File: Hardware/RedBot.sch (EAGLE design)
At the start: 67 parts, among them U1 ATMEGA328P, U2 TB6612FNG, U3 MIC5219 5V, U4 MIC5219 3.3V, U5 FT232RLSSOP, U6 7408SE, Y1 16MHz

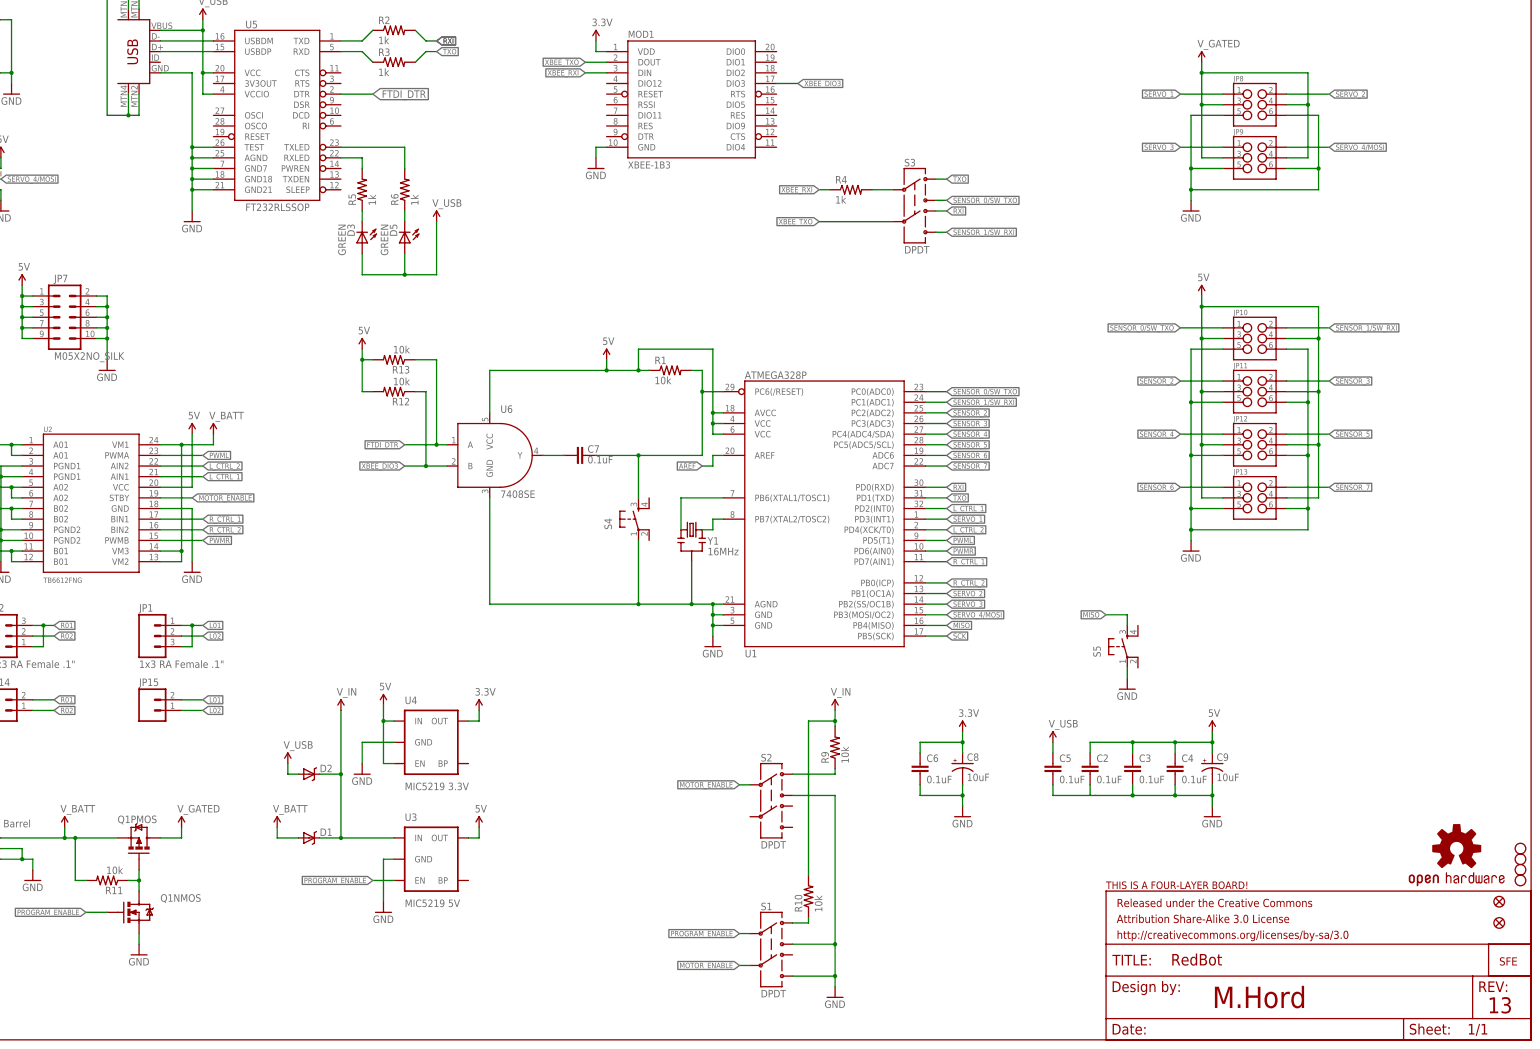
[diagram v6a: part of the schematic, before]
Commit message: Rollback design to current master
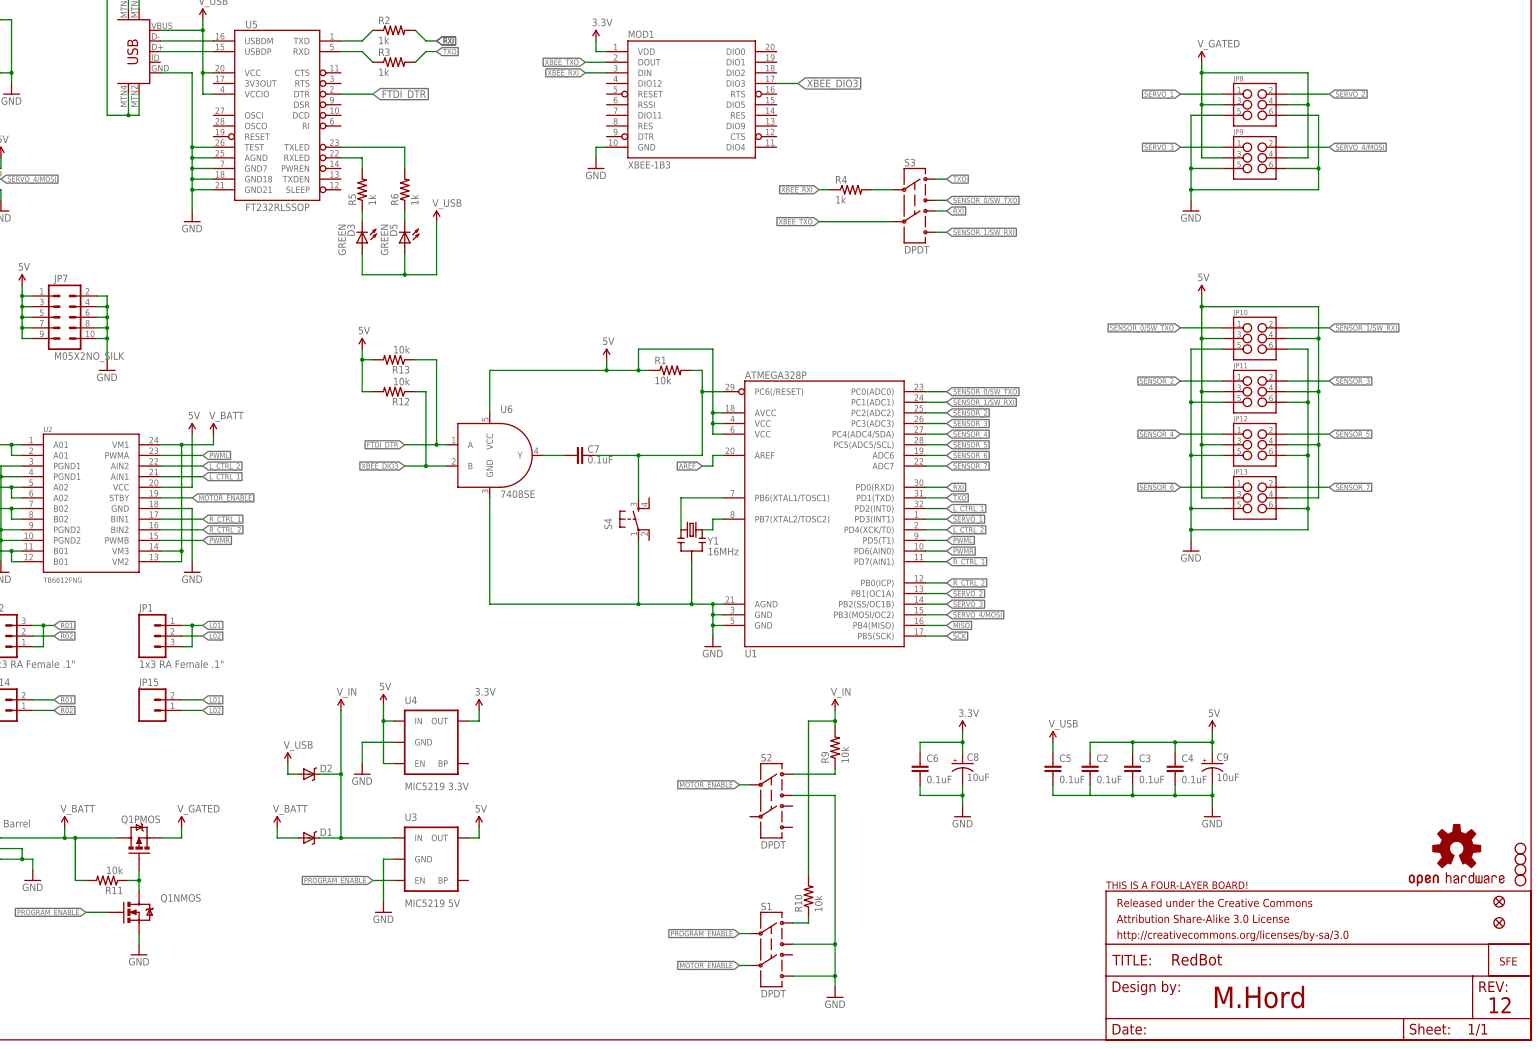
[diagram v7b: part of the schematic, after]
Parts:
- removed S5: (no value), SparkFun-Electromechanical:TAC_SWITCHSMD
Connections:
- net GND: no longer S5.1
- net MISO: no longer S5.3
- net V_BATT: now also Q1PMOS.D; no longer Q1PMOS.S
- net V_GATED: now also Q1PMOS.S; no longer Q1PMOS.D
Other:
- note added: "12"
- note removed: "13"
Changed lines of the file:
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@@
 <layer number="106" name="bPlate" color="7" fill="1" visible="no" active="yes"/>
 <layer number="107" name="Crop" color="7" fill="1" visible="no" active="yes"/>
-<layer number="108" name="tplace-old" color="10" fill="1" visible="yes" active="yes"/>
-<layer number="109" name="ref-old" color="11" fill="1" visible="yes" active="yes"/>
 <layer number="116" name="Patch_BOT" color="9" fill="4" visible="no" active="yes"/>
 <layer number="121" name="_tsilk" color="7" fill="1" visible="no" active="yes"/>
@@
 <part name="FID2" library="SparkFun-Aesthetics" deviceset="FIDUCIAL" device="UFIDUCIAL"/>
 <part name="U$22" library="SparkFun-Aesthetics" deviceset="5V" device="" value="V_USB"/>
-<part name="S5" library="SparkFun-Electromechanical" deviceset="TAC_SWITCH" device="SMD"/>
-<part name="GND12" library="SparkFun-Aesthetics" deviceset="GND" device=""/>
 </parts>
 <sheets>
@@
 <wire x1="0" y1="254" x2="0" y2="0" width="0.1524" layer="94"/>
 <text x="330.2" y="7.62" size="5.08" layer="94">M.Hord</text>
-<text x="395.986" y="6.35" size="3.81" layer="94">13</text>
+<text x="395.986" y="6.35" size="3.81" layer="94">12</text>
 </plain>
 <instances>
@@
 <instance part="JP15" gate="G$1" x="76.2" y="78.74"/>
 <instance part="Q1" gate="NMOS" x="73.66" y="30.48"/>
-<instance part="Q1" gate="PMOS" x="73.66" y="48.26" smashed="yes" rot="MR90">
-<attribute name="NAME" x="77.978" y="51.816" size="1.778" layer="95" rot="MR0"/>
-<attribute name="VALUE" x="73.66" y="53.34" size="1.778" layer="96" rot="MR90"/>
+<instance part="Q1" gate="PMOS" x="73.66" y="48.26" smashed="yes" rot="R90">
+<attribute name="NAME" x="69.342" y="51.816" size="1.778" layer="95"/>
+<attribute name="VALUE" x="73.66" y="53.34" size="1.778" layer="96" rot="R90"/>
 </instance>
 <instance part="GND19" gate="1" x="73.66" y="20.32"/>
@@
 <instance part="FID2" gate="G$1" x="398.78" y="27.94"/>
 <instance part="U$22" gate="G$1" x="144.78" y="195.58"/>
-<instance part="S5" gate="S" x="309.88" y="93.98" rot="R90"/>
-<instance part="GND12" gate="1" x="309.88" y="83.82"/>
 </instances>
 <busses>
@@
 <wire x1="20.32" y1="208.28" x2="15.24" y2="208.28" width="0.1524" layer="91"/>
 <label x="15.24" y="208.28" size="1.27" layer="95" rot="R180" xref="yes"/>
-</segment>
-<segment>
-<pinref part="S5" gate="S" pin="3"/>
-<wire x1="309.88" y1="99.06" x2="309.88" y2="101.6" width="0.1524" layer="91"/>
-<wire x1="309.88" y1="101.6" x2="304.8" y2="101.6" width="0.1524" layer="91"/>
-<label x="304.8" y="101.6" size="1.27" layer="95" rot="R180" xref="yes"/>
 </segment>
 </net>
@@
 <wire x1="27.94" y1="22.86" x2="27.94" y2="20.32" width="0.1524" layer="91"/>
 </segment>
-<segment>
-<pinref part="GND12" gate="1" pin="GND"/>
-<pinref part="S5" gate="S" pin="1"/>
-<wire x1="309.88" y1="86.36" x2="309.88" y2="88.9" width="0.1524" layer="91"/>
-</segment>
 </net>
 <net name="5V" class="0">
@@
 <wire x1="60.96" y1="38.1" x2="58.42" y2="38.1" width="0.1524" layer="91"/>
 <wire x1="58.42" y1="38.1" x2="58.42" y2="48.26" width="0.1524" layer="91"/>
+<pinref part="Q1" gate="PMOS" pin="D"/>
+<wire x1="58.42" y1="48.26" x2="68.58" y2="48.26" width="0.1524" layer="91"/>
+<junction x="58.42" y="48.26"/>
 <wire x1="40.64" y1="48.26" x2="55.88" y2="48.26" width="0.1524" layer="91"/>
 <pinref part="U$18" gate="G$1" pin="V_BATT"/>
@@
 <wire x1="55.88" y1="50.8" x2="55.88" y2="48.26" width="0.1524" layer="91"/>
 <junction x="55.88" y="48.26"/>
-<pinref part="Q1" gate="PMOS" pin="S"/>
-<wire x1="68.58" y1="48.26" x2="58.42" y2="48.26" width="0.1524" layer="91"/>
-<junction x="58.42" y="48.26"/>
 </segment>
 <segment>
@@
 <pinref part="MOD1" gate="G$1" pin="DIO3"/>
 <wire x1="226.06" y1="228.6" x2="231.14" y2="228.6" width="0.1524" layer="91"/>
-<label x="231.14" y="228.6" size="1.27" layer="95" xref="yes"/>
+<label x="231.14" y="228.6" size="1.778" layer="95" xref="yes"/>
 </segment>
 <segment>
@@
 <net name="V_GATED" class="0">
 <segment>
+<pinref part="Q1" gate="PMOS" pin="S"/>
+<wire x1="78.74" y1="48.26" x2="83.82" y2="48.26" width="0.1524" layer="91"/>
 <pinref part="V_GATE1" gate="G$1" pin="V_BATT"/>
 <wire x1="83.82" y1="50.8" x2="83.82" y2="48.26" width="0.1524" layer="91"/>
-<pinref part="Q1" gate="PMOS" pin="D"/>
-<wire x1="78.74" y1="48.26" x2="83.82" y2="48.26" width="0.1524" layer="91"/>
-</segment>
-<segment>
+</segment>
+<segment>

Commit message: Update boards to v13. - Flip MOSFET to gate power to Servo headers - Add button to pin 12 - change silk on LED to D13 LED - add some silk to the back
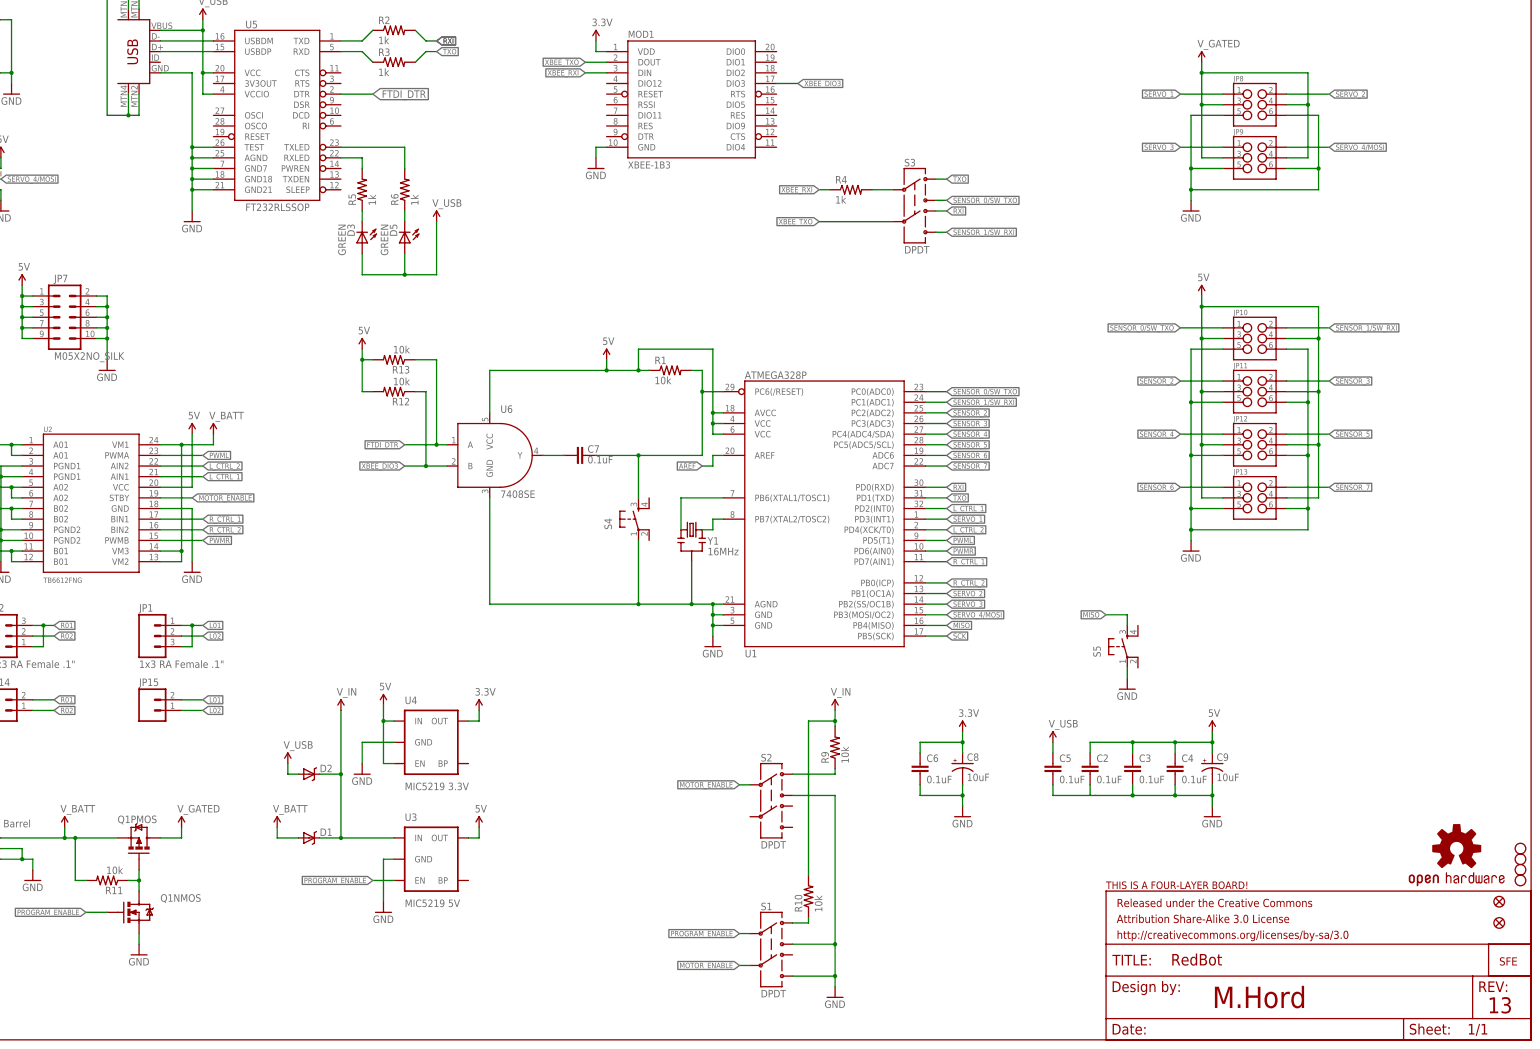
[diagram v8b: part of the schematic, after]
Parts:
- added S5: (no value), SparkFun-Electromechanical:TAC_SWITCHSMD
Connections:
- net GND: now also S5.1
- net MISO: now also S5.3
- net V_BATT: now also Q1PMOS.S; no longer Q1PMOS.D
- net V_GATED: now also Q1PMOS.D; no longer Q1PMOS.S
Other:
- note added: "13"
- note removed: "12"
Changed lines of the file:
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@@
 <layer number="106" name="bPlate" color="7" fill="1" visible="no" active="yes"/>
 <layer number="107" name="Crop" color="7" fill="1" visible="no" active="yes"/>
+<layer number="108" name="tplace-old" color="10" fill="1" visible="yes" active="yes"/>
+<layer number="109" name="ref-old" color="11" fill="1" visible="yes" active="yes"/>
 <layer number="116" name="Patch_BOT" color="9" fill="4" visible="no" active="yes"/>
 <layer number="121" name="_tsilk" color="7" fill="1" visible="no" active="yes"/>
@@
 <part name="FID2" library="SparkFun-Aesthetics" deviceset="FIDUCIAL" device="UFIDUCIAL"/>
 <part name="U$22" library="SparkFun-Aesthetics" deviceset="5V" device="" value="V_USB"/>
+<part name="S5" library="SparkFun-Electromechanical" deviceset="TAC_SWITCH" device="SMD"/>
+<part name="GND12" library="SparkFun-Aesthetics" deviceset="GND" device=""/>
 </parts>
 <sheets>
@@
 <wire x1="0" y1="254" x2="0" y2="0" width="0.1524" layer="94"/>
 <text x="330.2" y="7.62" size="5.08" layer="94">M.Hord</text>
-<text x="395.986" y="6.35" size="3.81" layer="94">12</text>
+<text x="395.986" y="6.35" size="3.81" layer="94">13</text>
 </plain>
 <instances>
@@
 <instance part="JP15" gate="G$1" x="76.2" y="78.74"/>
 <instance part="Q1" gate="NMOS" x="73.66" y="30.48"/>
-<instance part="Q1" gate="PMOS" x="73.66" y="48.26" smashed="yes" rot="R90">
-<attribute name="NAME" x="69.342" y="51.816" size="1.778" layer="95"/>
-<attribute name="VALUE" x="73.66" y="53.34" size="1.778" layer="96" rot="R90"/>
+<instance part="Q1" gate="PMOS" x="73.66" y="48.26" smashed="yes" rot="MR90">
+<attribute name="NAME" x="77.978" y="51.816" size="1.778" layer="95" rot="MR0"/>
+<attribute name="VALUE" x="73.66" y="53.34" size="1.778" layer="96" rot="MR90"/>
 </instance>
 <instance part="GND19" gate="1" x="73.66" y="20.32"/>
@@
 <instance part="FID2" gate="G$1" x="398.78" y="27.94"/>
 <instance part="U$22" gate="G$1" x="144.78" y="195.58"/>
+<instance part="S5" gate="S" x="309.88" y="93.98" rot="R90"/>
+<instance part="GND12" gate="1" x="309.88" y="83.82"/>
 </instances>
 <busses>
@@
 <wire x1="20.32" y1="208.28" x2="15.24" y2="208.28" width="0.1524" layer="91"/>
 <label x="15.24" y="208.28" size="1.27" layer="95" rot="R180" xref="yes"/>
+</segment>
+<segment>
+<pinref part="S5" gate="S" pin="3"/>
+<wire x1="309.88" y1="99.06" x2="309.88" y2="101.6" width="0.1524" layer="91"/>
+<wire x1="309.88" y1="101.6" x2="304.8" y2="101.6" width="0.1524" layer="91"/>
+<label x="304.8" y="101.6" size="1.27" layer="95" rot="R180" xref="yes"/>
 </segment>
 </net>
@@
 <wire x1="27.94" y1="22.86" x2="27.94" y2="20.32" width="0.1524" layer="91"/>
 </segment>
+<segment>
+<pinref part="GND12" gate="1" pin="GND"/>
+<pinref part="S5" gate="S" pin="1"/>
+<wire x1="309.88" y1="86.36" x2="309.88" y2="88.9" width="0.1524" layer="91"/>
+</segment>
 </net>
 <net name="5V" class="0">
@@
 <wire x1="60.96" y1="38.1" x2="58.42" y2="38.1" width="0.1524" layer="91"/>
 <wire x1="58.42" y1="38.1" x2="58.42" y2="48.26" width="0.1524" layer="91"/>
-<pinref part="Q1" gate="PMOS" pin="D"/>
-<wire x1="58.42" y1="48.26" x2="68.58" y2="48.26" width="0.1524" layer="91"/>
-<junction x="58.42" y="48.26"/>
 <wire x1="40.64" y1="48.26" x2="55.88" y2="48.26" width="0.1524" layer="91"/>
 <pinref part="U$18" gate="G$1" pin="V_BATT"/>
@@
 <wire x1="55.88" y1="50.8" x2="55.88" y2="48.26" width="0.1524" layer="91"/>
 <junction x="55.88" y="48.26"/>
+<pinref part="Q1" gate="PMOS" pin="S"/>
+<wire x1="68.58" y1="48.26" x2="58.42" y2="48.26" width="0.1524" layer="91"/>
+<junction x="58.42" y="48.26"/>
 </segment>
 <segment>
@@
 <pinref part="MOD1" gate="G$1" pin="DIO3"/>
 <wire x1="226.06" y1="228.6" x2="231.14" y2="228.6" width="0.1524" layer="91"/>
-<label x="231.14" y="228.6" size="1.778" layer="95" xref="yes"/>
+<label x="231.14" y="228.6" size="1.27" layer="95" xref="yes"/>
 </segment>
 <segment>
@@
 <net name="V_GATED" class="0">
 <segment>
-<pinref part="Q1" gate="PMOS" pin="S"/>
-<wire x1="78.74" y1="48.26" x2="83.82" y2="48.26" width="0.1524" layer="91"/>
 <pinref part="V_GATE1" gate="G$1" pin="V_BATT"/>
 <wire x1="83.82" y1="50.8" x2="83.82" y2="48.26" width="0.1524" layer="91"/>
-</segment>
-<segment>
+<pinref part="Q1" gate="PMOS" pin="D"/>
+<wire x1="78.74" y1="48.26" x2="83.82" y2="48.26" width="0.1524" layer="91"/>
+</segment>
+<segment>
